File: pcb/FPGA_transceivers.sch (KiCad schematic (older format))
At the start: 1 part

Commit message: schematic completed. Time for review
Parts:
- added C? (x2): 0.1u, symbol C
- added R?: R, symbol R
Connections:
- net PCIE_TX0_N: now reaches U?.A4 (MGTPTXN0_216)
- net PCIE_RX0_N: now reaches U?.A8 (MGTPRXN0_216)
- net PCIE_TX0_P: now reaches U?.B4 (MGTPTXP0_216)
- net PCIE_RX0_P: now reaches U?.B8 (MGTPRXP0_216)
- net SFP_RX_N: now reaches U?.C11 (MGTPRXN1_216)
- net SFP_TX_N: now reaches U?.C5 (MGTPTXN1_216)
- net SFP_RX_P: now reaches U?.D11 (MGTPRXP1_216)
- net SFP_TX_P: now reaches U?.D5 (MGTPTXP1_216)
- net SFP_CLK_N: now reaches U?.E10 (MGTREFCLK1N_216)
- net SFP_CLK_N: now also C?.1, C?.2
- net PCIE_CLK_N: now reaches U?.E6 (MGTREFCLK0N_216)
- net SFP_CLK_P: now reaches U?.F10 (MGTREFCLK1P_216)
- net SFP_CLK_P: now also C?.1, C?.2
- net PCIE_CLK_P: now reaches U?.F6 (MGTREFCLK0P_216)
- net at U?.F8 (MGTRREF_216): now also R?.1
- new net MGTAVTT: R?.2
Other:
- moved on the sheet: U?G
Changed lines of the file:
@@
 LIBS:valves
 LIBS:wbraun_ic_lib
-LIBS:xilinx-artix7
-LIBS:FMC_connector-cache
+LIBS:pgmfoot
 LIBS:artix7_pcie_pcb-cache
 EELAYER 25 0
@@
 $Descr A4 11693 8268
 encoding utf-8
-Sheet 7 10
+Sheet 7 12
 Title ""
 Date ""
@@
 L XC7Axxt-FGG484 U?
 U 7 1 56190228
-P 3850 3900
-F 0 "U?" H 2950 1300 60  0000 C CNN
-F 1 "XC7Axxt-FGG484" H 3250 6500 60  0000 C CNN
-F 2 "" H 3850 3950 60  0000 C CNN
-F 3 "" H 3850 3950 60  0000 C CNN
-	7    3850 3900
+P 3900 3850
+F 0 "U?" H 3000 1250 60  0000 C CNN
+F 1 "XC7Axxt-FGG484" H 3300 6450 60  0000 C CNN
+F 2 "" H 3900 3900 60  0000 C CNN
+F 3 "" H 3900 3900 60  0000 C CNN
+	7    3900 3850
 	1    0    0    -1
 $EndComp
+Text Label 5200 3800 0    60   ~ 0
+PCIE_CLK_P
+Text Label 5200 3900 0    60   ~ 0
+PCIE_CLK_N
+Text Label 5200 1400 0    60   ~ 0
+PCIE_TX0_P
+Text Label 5200 1500 0    60   ~ 0
+PCIE_TX0_N
+Text Label 5200 1700 0    60   ~ 0
+PCIE_RX0_P
+Text Label 5200 1800 0    60   ~ 0
+PCIE_RX0_N
+$Comp
+L R R?
+U 1 1 56510234
+P 5300 4650
+F 0 "R?" V 5380 4650 50  0000 C CNN
+F 1 "R" V 5300 4650 50  0000 C CNN
+F 2 "" V 5230 4650 30  0000 C CNN
+F 3 "" H 5300 4650 30  0000 C CNN
+	1    5300 4650
+	1    0    0    -1
+$EndComp
+Text HLabel 8000 1700 2    60   Input ~ 0
+PCIE_TX0_P
+Text HLabel 8000 1900 2    60   Input ~ 0
+PCIE_TX0_N
+Text HLabel 8000 2200 2    60   Input ~ 0
+PCIE_RX0_P
+Text HLabel 8000 2400 2    60   Input ~ 0
+PCIE_RX0_N
+Text HLabel 8000 2700 2    60   Input ~ 0
+PCIE_CLK_P
+Text HLabel 8000 2900 2    60   Input ~ 0
+PCIE_CLK_N
+Text Label 7700 1700 2    60   ~ 0
+PCIE_TX0_P
+Text Label 7700 1900 2    60   ~ 0
+PCIE_TX0_N
+Text Label 7700 2200 2    60   ~ 0
+PCIE_RX0_P
+Text Label 7700 2400 2    60   ~ 0
+PCIE_RX0_N
+Text Label 7700 2700 2    60   ~ 0
+PCIE_CLK_P
+Text Label 7700 2900 2    60   ~ 0
+PCIE_CLK_N
+Wire Wire Line
+	5100 3800 5200 3800
+Wire Wire Line
+	5100 3900 5200 3900
+Wire Wire Line
+	5100 1400 5200 1400
+Wire Wire Line
+	5100 1500 5200 1500
+Wire Wire Line
+	5100 1700 5200 1700
+Wire Wire Line
+	5100 1800 5200 1800
+Wire Wire Line
+	5600 4900 5300 4900
+Wire Wire Line
+	5300 4900 5300 4800
+Wire Wire Line
+	5100 4400 5300 4400
+Wire Wire Line
+	5300 4400 5300 4500
+Wire Wire Line
+	8000 1700 7700 1700
+Wire Wire Line
+	8000 1900 7700 1900
+Wire Wire Line
+	8000 2200 7700 2200
+Wire Wire Line
+	8000 2400 7700 2400
+Wire Wire Line
+	8000 2700 7700 2700
+Wire Wire Line
+	8000 2900 7700 2900
+Wire Wire Line
+	5100 2000 5200 2000
+Wire Wire Line
+	5100 2100 5200 2100
+Wire Wire Line
+	5100 2300 5200 2300
+Wire Wire Line
+	5100 2400 5200 2400
+Text Label 5200 2000 0    60   ~ 0
+SFP_TX_P
+Text Label 5200 2100 0    60   ~ 0
+SFP_TX_N
+Text Label 5200 2300 0    60   ~ 0
+SFP_RX_P
+Text Label 5200 2400 0    60   ~ 0
+SFP_RX_N
+Wire Wire Line
+	5100 4100 5200 4100
+Wire Wire Line
+	5100 4200 5200 4200
+Text Label 5200 4100 0    60   ~ 0
+SFP_CLK_P
+Text Label 5200 4200 0    60   ~ 0
+SFP_CLK_N
+Wire Wire Line
+	8000 3200 7700 3200
+Wire Wire Line
+	8000 3400 7700 3400
+Wire Wire Line
+	8000 3700 7700 3700
+Wire Wire Line
+	8000 3900 7700 3900
+Wire Wire Line
+	8000 4200 7700 4200
+Wire Wire Line
+	8000 4400 7700 4400
+Text Label 7700 3200 2    60   ~ 0
+SFP_TX_P
+Text Label 7700 3400 2    60   ~ 0
+SFP_TX_N
+Text Label 7700 3700 2    60   ~ 0
+SFP_RX_P
+Text Label 7700 3900 2    60   ~ 0
+SFP_RX_N
+Text Label 7700 4200 2    60   ~ 0
+SFP_CLK_P
+Text Label 7700 4400 2    60   ~ 0
+SFP_CLK_N
+Text HLabel 8000 3200 2    60   Input ~ 0
+SFP_TX_P
+Text HLabel 8000 3400 2    60   Input ~ 0
+SFP_TX_N
+Text HLabel 8000 3700 2    60   Input ~ 0
+SFP_RX_P
+Text HLabel 8000 3900 2    60   Input ~ 0
+SFP_RX_N
+Text HLabel 8400 4200 2    60   Input ~ 0
+SFP_CLK_P
+Text HLabel 8400 4400 2    60   Input ~ 0
+SFP_CLK_N
+$Comp
+L C C?
+U 1 1 565FA006
+P 8150 4400
+F 0 "C?" H 8175 4500 50  0000 L CNN
+F 1 "0.1u" H 8175 4300 50  0000 L CNN
+F 2 "" H 8188 4250 30  0000 C CNN
+F 3 "" H 8150 4400 60  0000 C CNN
+	1    8150 4400
+	0    1    1    0
+$EndComp
+$Comp
+L C C?
+U 1 1 565FA058
+P 8150 4200
+F 0 "C?" H 8175 4300 50  0000 L CNN
+F 1 "0.1u" H 8175 4100 50  0000 L CNN
+F 2 "" H 8188 4050 30  0000 C CNN
+F 3 "" H 8150 4200 60  0000 C CNN
+	1    8150 4200
+	0    1    1    0
+$EndComp
+Wire Wire Line
+	8300 4200 8400 4200
+Wire Wire Line
+	8300 4400 8400 4400
+Text GLabel 5600 4900 2    60   Input ~ 0
+MGTAVTT
 $EndSCHEMATC

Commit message: Added part numbers and updated schematic
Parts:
- gave numbers to parts that had none: 4
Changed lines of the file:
@@
 $EndDescr
 $Comp
-L XC7Axxt-FGG484 U?
+L XC7Axxt-FGG484 U401
 U 7 1 56190228
 P 3900 3850
-F 0 "U?" H 3000 1250 60  0000 C CNN
+F 0 "U401" H 3000 1250 60  0000 C CNN
 F 1 "XC7Axxt-FGG484" H 3300 6450 60  0000 C CNN
 F 2 "" H 3900 3900 60  0000 C CNN
@@
 PCIE_RX0_N
 $Comp
-L R R?
+L R R701
 U 1 1 56510234
 P 5300 4650
-F 0 "R?" V 5380 4650 50  0000 C CNN
+F 0 "R701" V 5380 4650 50  0000 C CNN
 F 1 "R" V 5300 4650 50  0000 C CNN
 F 2 "" V 5230 4650 30  0000 C CNN
@@
 SFP_CLK_N
 $Comp
-L C C?
+L C C702
 U 1 1 565FA006
 P 8150 4400
-F 0 "C?" H 8175 4500 50  0000 L CNN
+F 0 "C702" H 8175 4500 50  0000 L CNN
 F 1 "0.1u" H 8175 4300 50  0000 L CNN
 F 2 "" H 8188 4250 30  0000 C CNN
@@
 $EndComp
 $Comp
-L C C?
+L C C701
 U 1 1 565FA058
 P 8150 4200
-F 0 "C?" H 8175 4300 50  0000 L CNN
+F 0 "C701" H 8175 4300 50  0000 L CNN
 F 1 "0.1u" H 8175 4100 50  0000 L CNN
 F 2 "" H 8188 4050 30  0000 C CNN

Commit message: mostly done with component placement
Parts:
- C701, C702: footprint (none) -> wbraun_smd:C_0402
- R701: footprint (none) -> wbraun_smd:R_0402
- U401: footprint (none) -> wbraun_smd:BGA_484_22x22_FULLARRAY_1MM
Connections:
- net SFP_CLK_N: no longer C702.2, U401.E10 (MGTREFCLK1N_216)
- net SFP_CLK_P: no longer C701.2, U401.F10 (MGTREFCLK1P_216)
- new net SFP_CLK_C_N: C702.2, U401.E10 (MGTREFCLK1N_216)
- new net SFP_CLK_C_P: C701.2, U401.F10 (MGTREFCLK1P_216)
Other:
- moved on the sheet: C702
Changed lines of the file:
@@
 F 0 "U401" H 3000 1250 60  0000 C CNN
 F 1 "XC7Axxt-FGG484" H 3300 6450 60  0000 C CNN
-F 2 "" H 3900 3900 60  0000 C CNN
+F 2 "wbraun_smd:BGA_484_22x22_FULLARRAY_1MM" H 3900 3900 60  0001 C CNN
 F 3 "" H 3900 3900 60  0000 C CNN
 	7    3900 3850
@@
 F 0 "R701" V 5380 4650 50  0000 C CNN
 F 1 "R" V 5300 4650 50  0000 C CNN
-F 2 "" V 5230 4650 30  0000 C CNN
+F 2 "wbraun_smd:R_0402" V 5230 4650 30  0001 C CNN
 F 3 "" H 5300 4650 30  0000 C CNN
 	1    5300 4650
@@
 	5100 4200 5200 4200
 Text Label 5200 4100 0    60   ~ 0
-SFP_CLK_P
+SFP_CLK_C_P
 Text Label 5200 4200 0    60   ~ 0
-SFP_CLK_N
+SFP_CLK_C_N
 Wire Wire Line
 	8000 3200 7700 3200
@@
 	8000 4200 7700 4200
 Wire Wire Line
-	8000 4400 7700 4400
+	8000 4650 7700 4650
 Text Label 7700 3200 2    60   ~ 0
 SFP_TX_P
@@
 SFP_RX_N
 Text Label 7700 4200 2    60   ~ 0
-SFP_CLK_P
-Text Label 7700 4400 2    60   ~ 0
-SFP_CLK_N
+SFP_CLK_C_P
+Text Label 7700 4650 2    60   ~ 0
+SFP_CLK_C_N
 Text HLabel 8000 3200 2    60   Input ~ 0
 SFP_TX_P
@@
 Text HLabel 8400 4200 2    60   Input ~ 0
 SFP_CLK_P
-Text HLabel 8400 4400 2    60   Input ~ 0
+Text HLabel 8400 4650 2    60   Input ~ 0
 SFP_CLK_N
 $Comp
 L C C702
 U 1 1 565FA006
-P 8150 4400
-F 0 "C702" H 8175 4500 50  0000 L CNN
-F 1 "0.1u" H 8175 4300 50  0000 L CNN
-F 2 "" H 8188 4250 30  0000 C CNN
-F 3 "" H 8150 4400 60  0000 C CNN
-	1    8150 4400
+P 8150 4650
+F 0 "C702" H 8175 4750 50  0000 L CNN
+F 1 "0.1u" H 8175 4550 50  0000 L CNN
+F 2 "wbraun_smd:C_0402" H 8188 4500 30  0001 C CNN
+F 3 "" H 8150 4650 60  0000 C CNN
+	1    8150 4650
 	0    1    1    0
 $EndComp
@@
 F 0 "C701" H 8175 4300 50  0000 L CNN
 F 1 "0.1u" H 8175 4100 50  0000 L CNN
-F 2 "" H 8188 4050 30  0000 C CNN
+F 2 "wbraun_smd:C_0402" H 8188 4050 30  0001 C CNN
 F 3 "" H 8150 4200 60  0000 C CNN
 	1    8150 4200
@@
 	8300 4200 8400 4200
 Wire Wire Line
-	8300 4400 8400 4400
+	8300 4650 8400 4650
 Text GLabel 5600 4900 2    60   Input ~ 0
 MGTAVTT

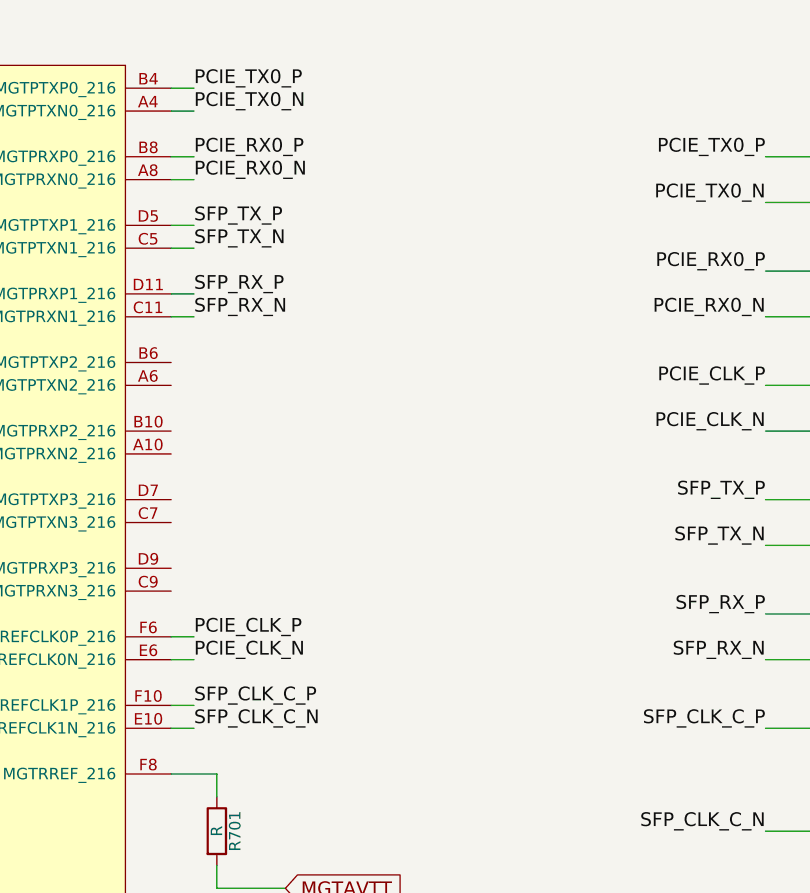
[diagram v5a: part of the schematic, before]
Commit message: Finished most of the routing, removed DDR-3
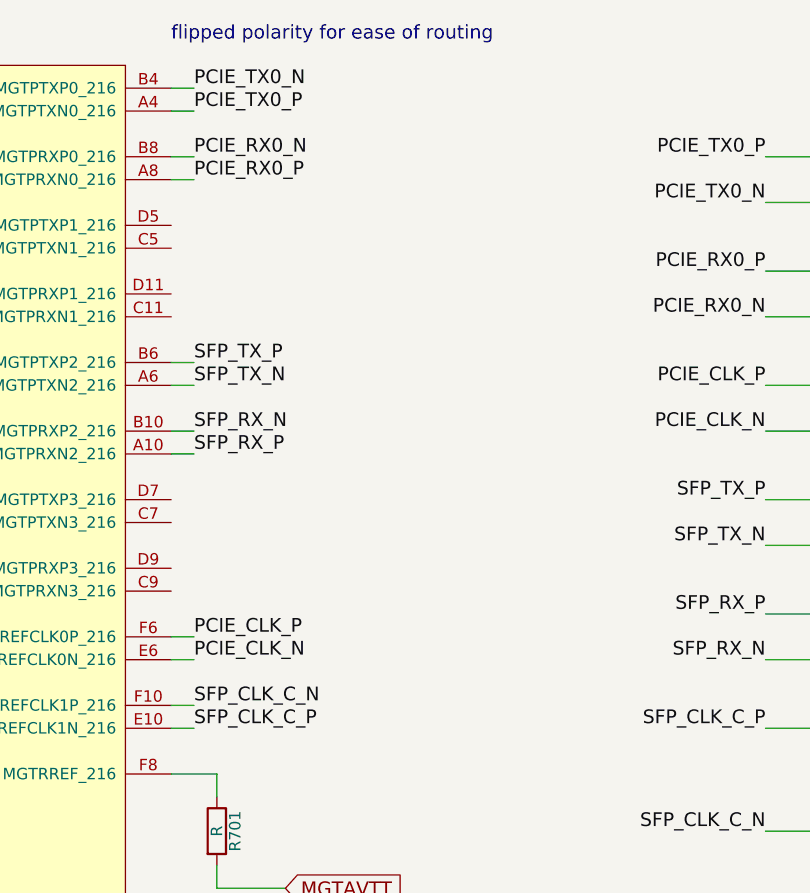
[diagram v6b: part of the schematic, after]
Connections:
- net PCIE_RX0_N: now also U401.B8 (MGTPRXP0_216); no longer U401.A8 (MGTPRXN0_216)
- net PCIE_RX0_P: now also U401.A8 (MGTPRXN0_216); no longer U401.B8 (MGTPRXP0_216)
- net PCIE_TX0_N: now also U401.B4 (MGTPTXP0_216); no longer U401.A4 (MGTPTXN0_216)
- net PCIE_TX0_P: now also U401.A4 (MGTPTXN0_216); no longer U401.B4 (MGTPTXP0_216)
- net SFP_CLK_C_N: now also U401.F10 (MGTREFCLK1P_216); no longer U401.E10 (MGTREFCLK1N_216)
- net SFP_CLK_C_P: now also U401.E10 (MGTREFCLK1N_216); no longer U401.F10 (MGTREFCLK1P_216)
- net SFP_RX_N: now also U401.B10 (MGTPRXP2_216); no longer U401.C11 (MGTPRXN1_216)
- net SFP_RX_P: now also U401.A10 (MGTPRXN2_216); no longer U401.D11 (MGTPRXP1_216)
- net SFP_TX_N: now also U401.A6 (MGTPTXN2_216); no longer U401.C5 (MGTPTXN1_216)
- net SFP_TX_P: now also U401.B6 (MGTPTXP2_216); no longer U401.D5 (MGTPTXP1_216)
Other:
- note added: "flipped polarity for ease of routing"
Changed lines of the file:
@@
 $Descr A4 11693 8268
 encoding utf-8
-Sheet 7 13
+Sheet 7 11
 Title ""
 Date ""
@@
 Text Label 5200 3900 0    60   ~ 0
 PCIE_CLK_N
+Text Label 5200 1500 0    60   ~ 0
+PCIE_TX0_P
 Text Label 5200 1400 0    60   ~ 0
-PCIE_TX0_P
-Text Label 5200 1500 0    60   ~ 0
 PCIE_TX0_N
+Text Label 5200 1800 0    60   ~ 0
+PCIE_RX0_P
 Text Label 5200 1700 0    60   ~ 0
-PCIE_RX0_P
-Text Label 5200 1800 0    60   ~ 0
 PCIE_RX0_N
 $Comp
@@
 	8000 2900 7700 2900
 Wire Wire Line
-	5100 2000 5200 2000
+	5100 2600 5200 2600
 Wire Wire Line
-	5100 2100 5200 2100
+	5100 2700 5200 2700
 Wire Wire Line
-	5100 2300 5200 2300
+	5100 2900 5200 2900
 Wire Wire Line
-	5100 2400 5200 2400
-Text Label 5200 2000 0    60   ~ 0
+	5100 3000 5200 3000
+Text Label 5200 2600 0    60   ~ 0
 SFP_TX_P
-Text Label 5200 2100 0    60   ~ 0
+Text Label 5200 2700 0    60   ~ 0
 SFP_TX_N
-Text Label 5200 2300 0    60   ~ 0
+Text Label 5200 3000 0    60   ~ 0
 SFP_RX_P
-Text Label 5200 2400 0    60   ~ 0
+Text Label 5200 2900 0    60   ~ 0
 SFP_RX_N
 Wire Wire Line
@@
 Wire Wire Line
 	5100 4200 5200 4200
+Text Label 5200 4200 0    60   ~ 0
+SFP_CLK_C_P
 Text Label 5200 4100 0    60   ~ 0
-SFP_CLK_C_P
-Text Label 5200 4200 0    60   ~ 0
 SFP_CLK_C_N
 Wire Wire Line
@@
 Text GLabel 5600 4900 2    60   Input ~ 0
 MGTAVTT
+Text Notes 5100 1200 0    60   ~ 0
+flipped polarity for ease of routing
 $EndSCHEMATC

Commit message: Ready for fab
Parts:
- U401: symbol XC7Axxt-FGG484 -> XC7Axxt-FGG484-RESCUE-artix7_pcie_pcb
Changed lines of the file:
@@
 EESchema Schematic File Version 2
+LIBS:artix7_pcie_pcb-rescue
 LIBS:power
 LIBS:device
@@
 LIBS:valves
 LIBS:wbraun_ic_lib
-LIBS:pgmfoot
 LIBS:artix7_pcie_pcb-cache
 EELAYER 25 0
@@
 $EndDescr
 $Comp
-L XC7Axxt-FGG484 U401
+L XC7Axxt-FGG484-RESCUE-artix7_pcie_pcb U401
 U 7 1 56190228
 P 3900 3850
